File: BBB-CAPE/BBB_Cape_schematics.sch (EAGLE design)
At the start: 81 parts, among them IC1 EEPROM-I2CSMD, SW2 219-02

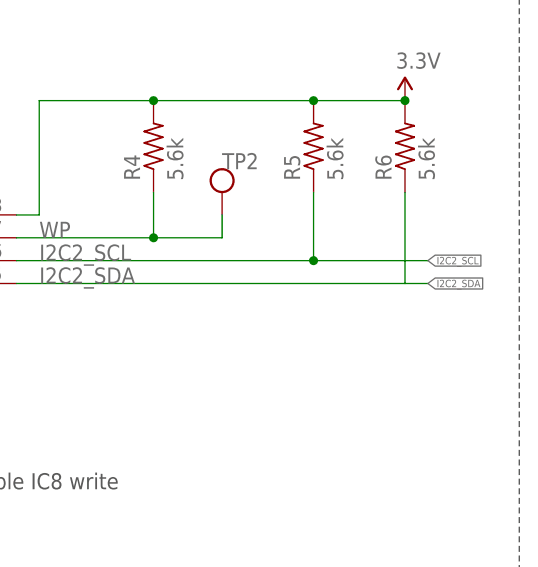
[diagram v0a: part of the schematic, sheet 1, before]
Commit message: Placement of components in BBB_Cape_schematics.brd, removed ERC erros in BBB_Cape_schematics.sch and Add sign in INA129 to identify pin no 1 in Components.lbr
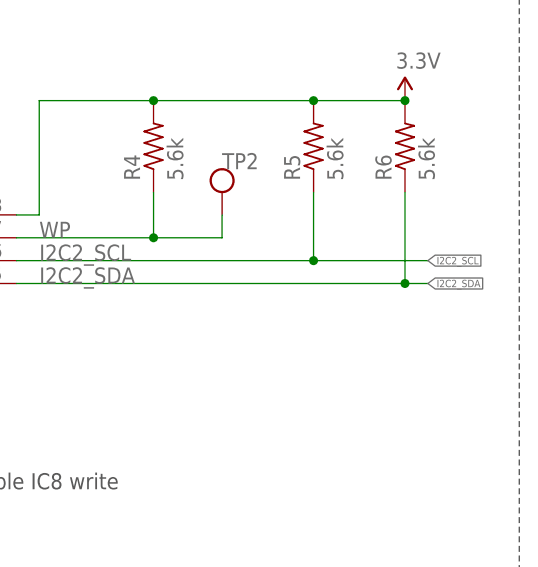
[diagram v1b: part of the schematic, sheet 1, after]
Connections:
- net N$23: now also U$17.P$1; no longer U$16.P$1
- net N$24: now also U$16.P$1; no longer U$17.P$1
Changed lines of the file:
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@@
 <setting verticaltext="up"/>
 </settings>
-<grid distance="0.1" unitdist="inch" unit="inch" style="lines" multiple="1" display="yes" altdistance="0.01" altunitdist="inch" altunit="inch"/>
+<grid distance="0.1" unitdist="inch" unit="inch" style="lines" multiple="1" display="no" altdistance="0.01" altunitdist="inch" altunit="inch"/>
 <layers>
 <layer number="1" name="Top" color="4" fill="1" visible="yes" active="no"/>
@@
 <part name="U$14" library="Components" deviceset="LMP2021" device=""/>
 <part name="U$15" library="SparkFun-Aesthetics" deviceset="5V" device=""/>
+<part name="U$17" library="Components" deviceset="PAD" device=""/>
 <part name="U$16" library="Components" deviceset="PAD" device=""/>
-<part name="U$17" library="Components" deviceset="PAD" device=""/>
 <part name="U$18" library="Components" deviceset="PAD" device=""/>
 <part name="U$19" library="Components" deviceset="ADS1252" device=""/>
@@
 <label x="99.06" y="215.9" size="1.778" layer="95"/>
 <wire x1="96.52" y1="215.9" x2="139.7" y2="215.9" width="0.1524" layer="91"/>
+<label x="142.24" y="215.9" size="0.8128" layer="95" xref="yes"/>
 <pinref part="R6" gate="G$1" pin="1"/>
+<wire x1="139.7" y1="215.9" x2="142.24" y2="215.9" width="0.1524" layer="91"/>
 <wire x1="139.7" y1="226.06" x2="139.7" y2="215.9" width="0.1524" layer="91"/>
-<label x="142.24" y="215.9" size="0.8128" layer="95" xref="yes"/>
-<wire x1="139.7" y1="215.9" x2="142.24" y2="215.9" width="0.1524" layer="91"/>
+<junction x="139.7" y="215.9"/>
 </segment>
 </net>
@@
 <instance part="P+10" gate="1" x="307.34" y="200.66"/>
 <instance part="GND19" gate="1" x="307.34" y="160.02"/>
-<instance part="U$16" gate="G$1" x="68.58" y="205.74"/>
-<instance part="U$17" gate="G$1" x="68.58" y="170.18"/>
+<instance part="U$17" gate="G$1" x="68.58" y="205.74"/>
+<instance part="U$16" gate="G$1" x="68.58" y="170.18"/>
 <instance part="U$18" gate="G$1" x="45.72" y="50.8"/>
 <instance part="TP_ECG_LPF" gate="G$1" x="330.2" y="172.72" rot="R270"/>
@@
 </segment>
 <segment>
-<pinref part="C3" gate="G$1" pin="2"/>
-<pinref part="GND8" gate="1" pin="GND"/>
-<wire x1="121.92" y1="154.94" x2="121.92" y2="149.86" width="0.1524" layer="91"/>
-</segment>
-<segment>
 <pinref part="GND15" gate="1" pin="GND"/>
 <wire x1="213.36" y1="149.86" x2="213.36" y2="152.4" width="0.1524" layer="91"/>
@@
 <pinref part="GND27" gate="1" pin="GND"/>
 <wire x1="187.96" y1="147.32" x2="187.96" y2="144.78" width="0.1524" layer="91"/>
+</segment>
+<segment>
+<pinref part="C3" gate="G$1" pin="2"/>
+<pinref part="GND8" gate="1" pin="GND"/>
+<wire x1="121.92" y1="154.94" x2="121.92" y2="149.86" width="0.1524" layer="91"/>
 </segment>
 </net>
@@
 <net name="N$23" class="0">
 <segment>
-<pinref part="U$16" gate="G$1" pin="P$1"/>
+<pinref part="U$17" gate="G$1" pin="P$1"/>
 <pinref part="R11" gate="G$1" pin="1"/>
 <wire x1="86.36" y1="205.74" x2="91.44" y2="205.74" width="0.1524" layer="91"/>
@@
 <net name="N$24" class="0">
 <segment>
-<pinref part="U$17" gate="G$1" pin="P$1"/>
+<pinref part="U$16" gate="G$1" pin="P$1"/>
 <pinref part="R12" gate="G$1" pin="1"/>
 <wire x1="86.36" y1="170.18" x2="91.44" y2="170.18" width="0.1524" layer="91"/>

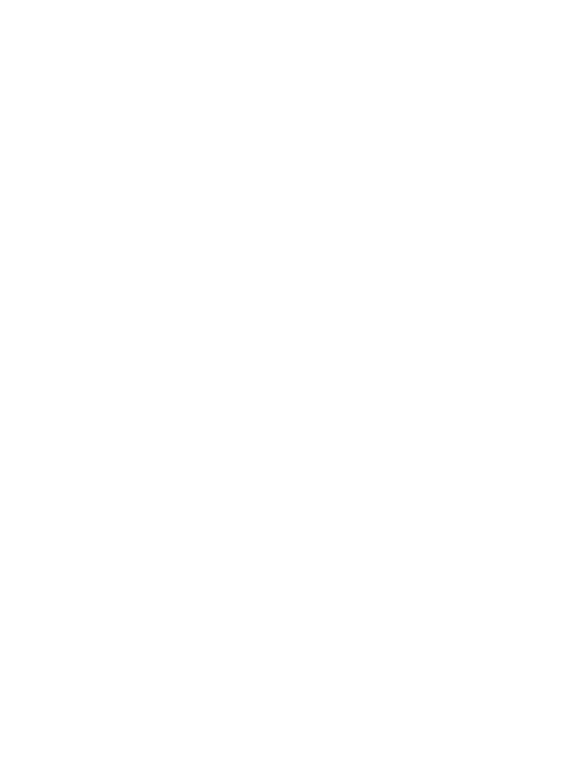
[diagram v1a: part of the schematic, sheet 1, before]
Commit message: Add 4D LCD to BBB_Cape_schematics.sch
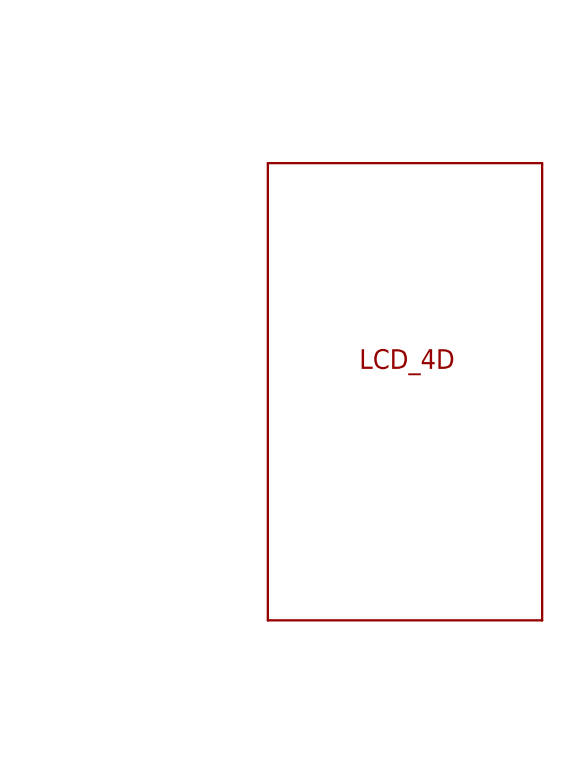
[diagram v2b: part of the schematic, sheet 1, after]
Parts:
- added U$25: LCD_4D, Components:LCD_4D
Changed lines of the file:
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@@
 <setting verticaltext="up"/>
 </settings>
-<grid distance="0.1" unitdist="inch" unit="inch" style="lines" multiple="1" display="no" altdistance="0.01" altunitdist="inch" altunit="inch"/>
+<grid distance="0.1" unitdist="inch" unit="inch" style="lines" multiple="1" display="yes" altdistance="0.01" altunitdist="inch" altunit="inch"/>
 <layers>
 <layer number="1" name="Top" color="4" fill="1" visible="yes" active="no"/>
@@
 <part name="C12" library="rcl" deviceset="C-US" device="C1206" value="0.10uF"/>
 <part name="GND30" library="supply1" deviceset="GND" device=""/>
+<part name="U$25" library="Components" deviceset="LCD_4D" device=""/>
 </parts>
 <sheets>
@@
 </instance>
 <instance part="SW2" gate="G$1" x="33.02" y="210.82" rot="R270"/>
+<instance part="U$25" gate="G$1" x="269.24" y="142.24"/>
 </instances>
 <busses>

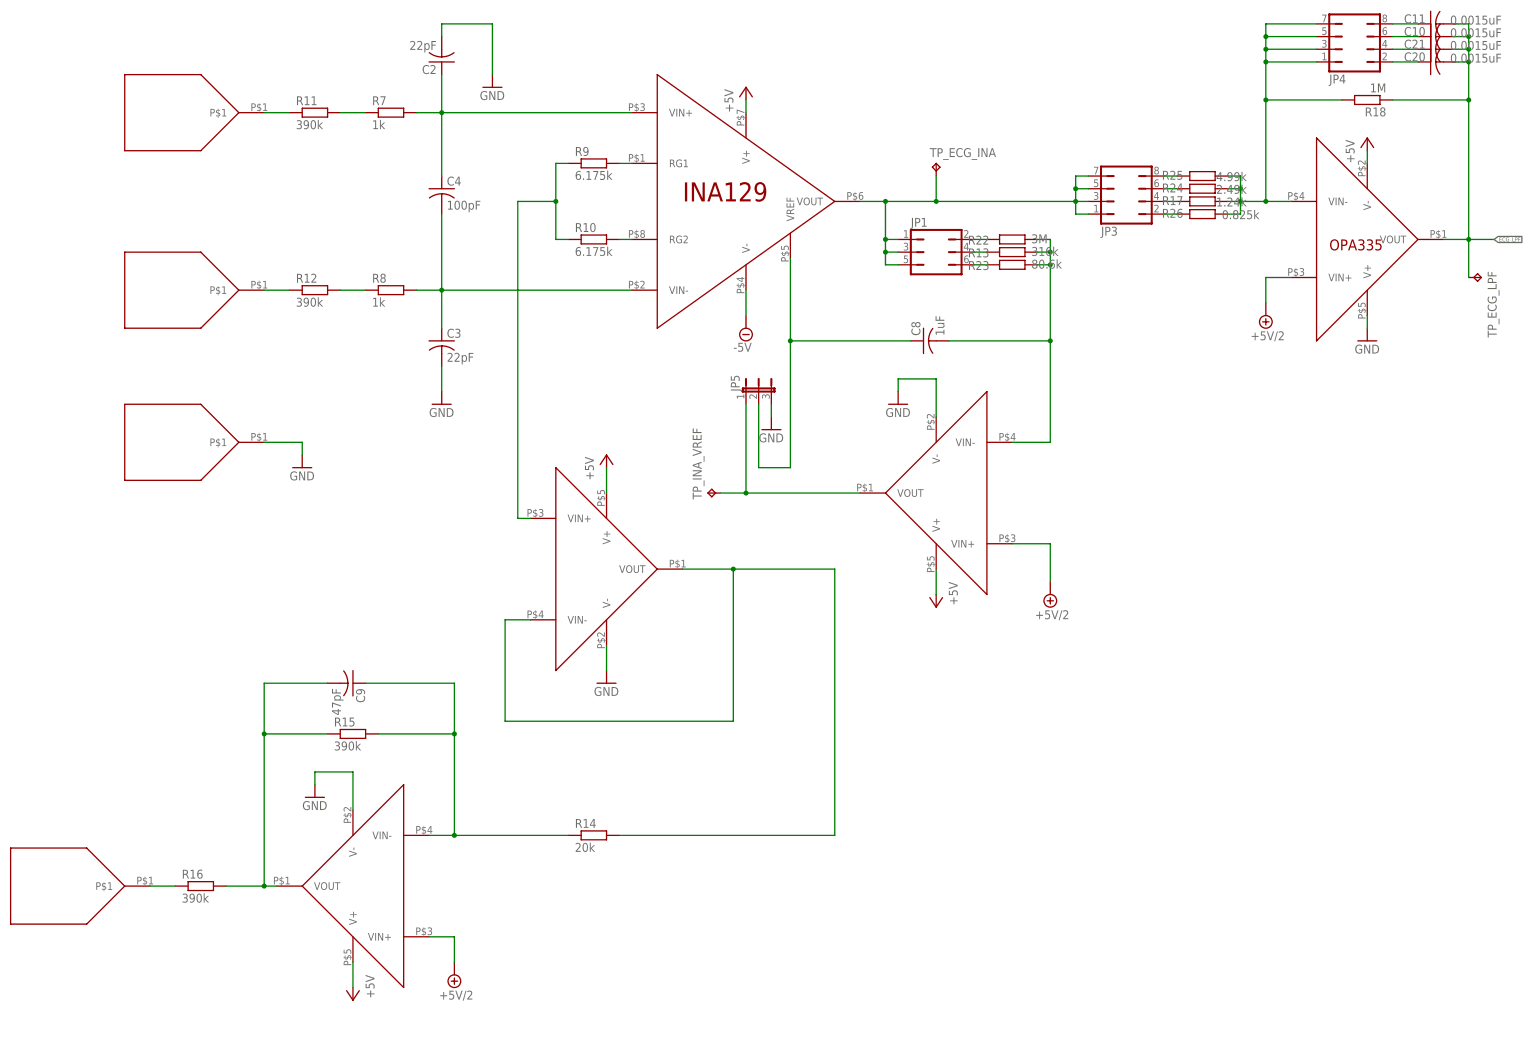
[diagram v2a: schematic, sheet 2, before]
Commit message: Replace all LMP2021 with OPA335 in BBB_Cape_schematics.sch
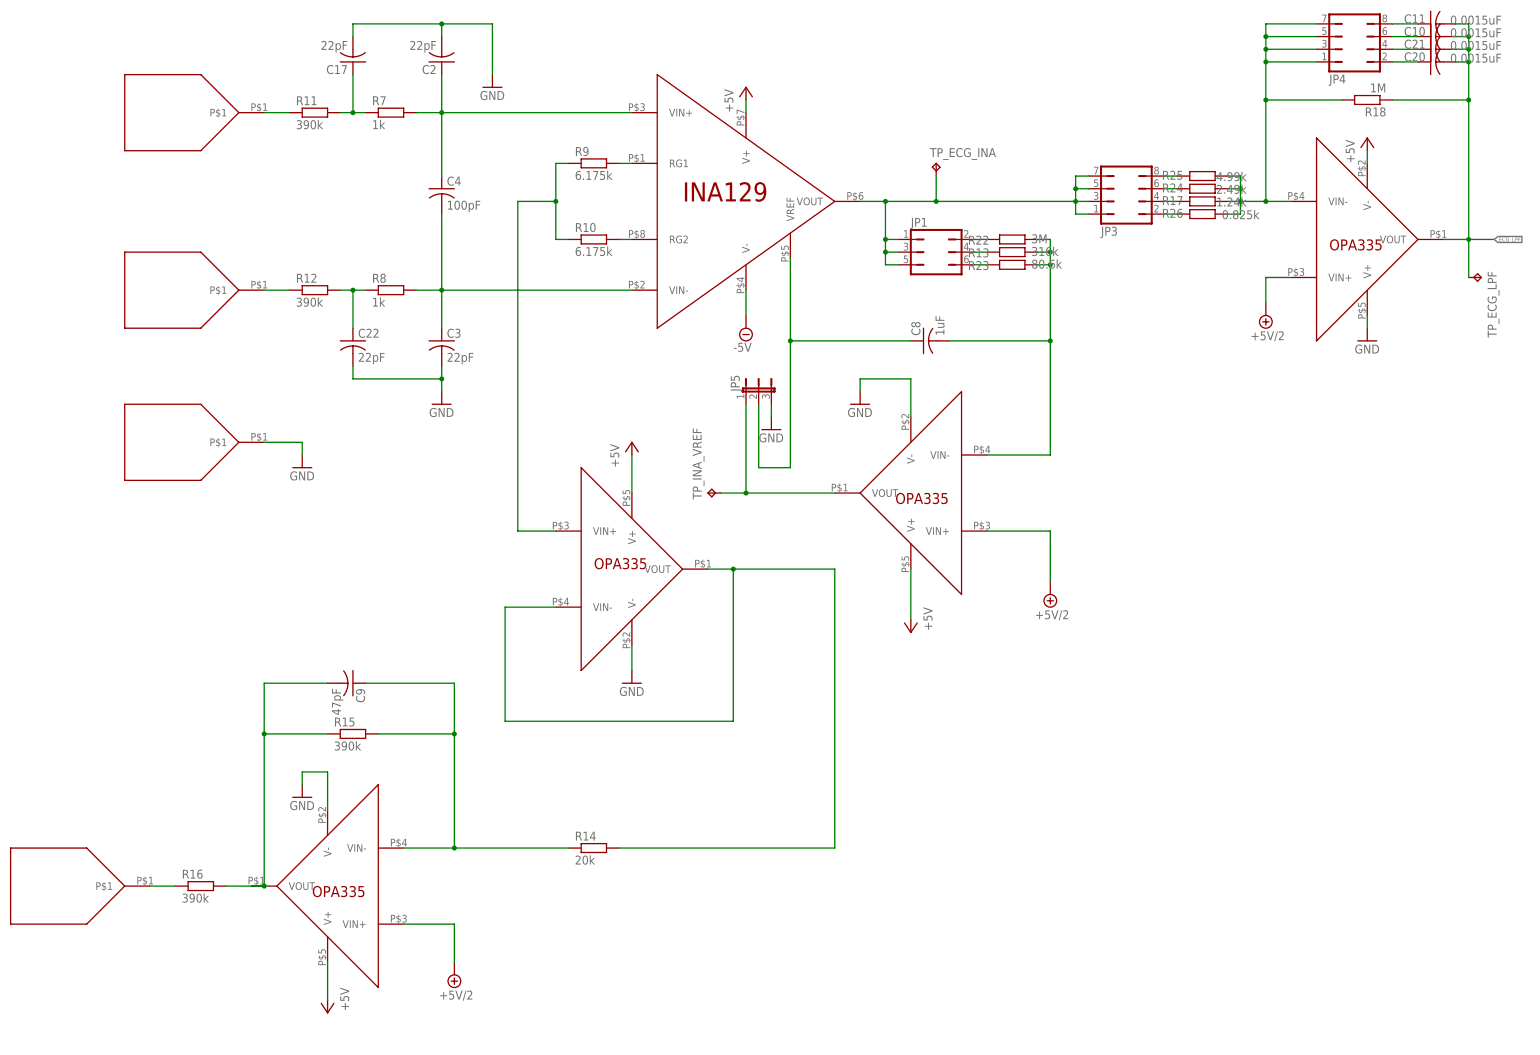
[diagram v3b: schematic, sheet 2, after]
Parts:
- added C17, C22: 22pF, rcl:C-USC1206
- U$11, U$12, U$14, U$9: value LMP2021 -> OPA335; device Components:LMP2021 -> Components:OPA335
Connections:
- net GND: now also C17.2, C22.2
- net N$7: now also C17.1
- net N$8: now also C22.1
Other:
- moved on the sheet: R14, TP2_MIN5V

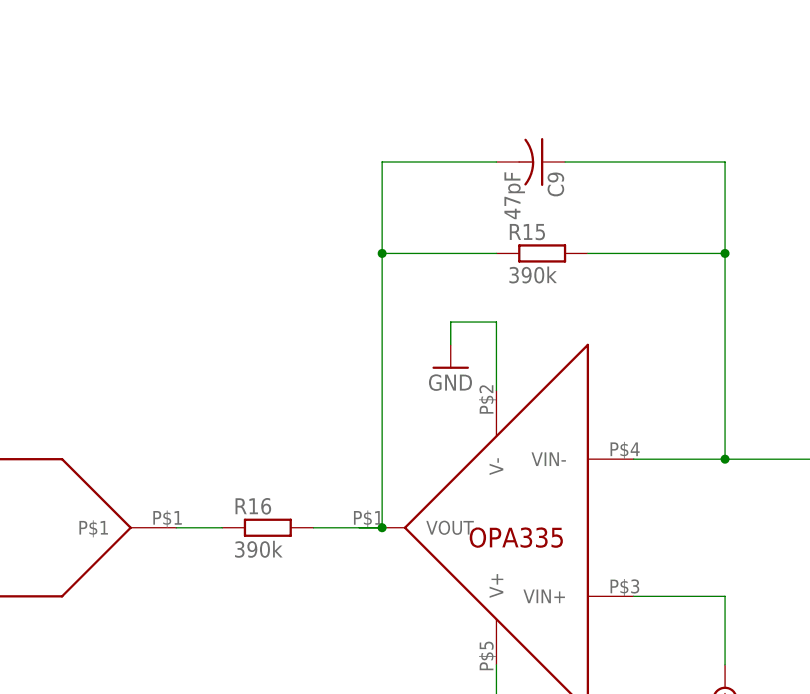
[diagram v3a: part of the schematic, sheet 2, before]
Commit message: Change +5V signal to 5V signal in BBB_Cape_schematics.sch and Update 12MHz crystal package in BBB_Cape_schematics.brd
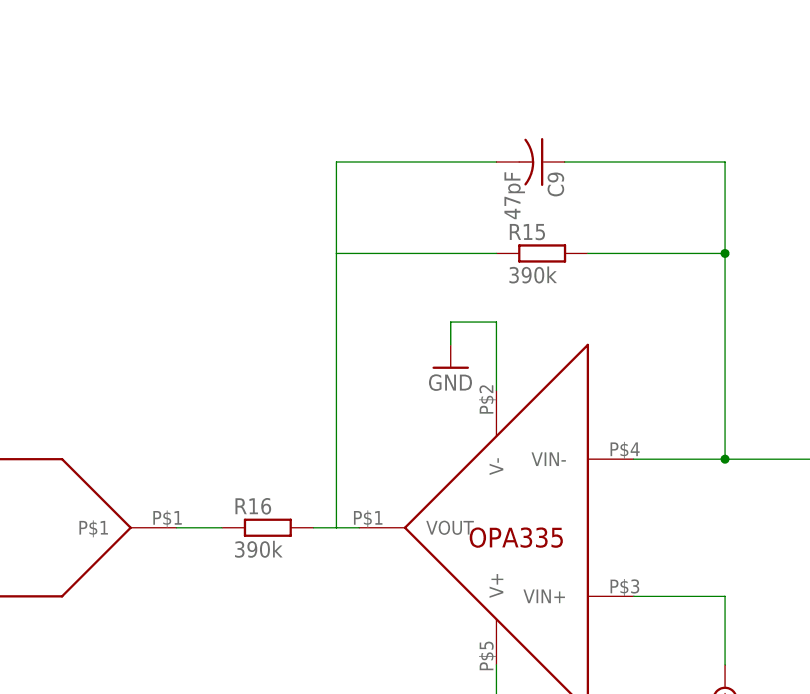
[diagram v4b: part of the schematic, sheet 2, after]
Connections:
- net +5V: no longer C13.1, U$21.VIN
- net 5V: now also C13.1, U$21.VIN
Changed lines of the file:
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@@
 <setting verticaltext="up"/>
 </settings>
-<grid distance="0.1" unitdist="inch" unit="inch" style="lines" multiple="1" display="yes" altdistance="0.01" altunitdist="inch" altunit="inch"/>
+<grid distance="0.1" unitdist="inch" unit="inch" style="lines" multiple="1" display="no" altdistance="0.01" altunitdist="inch" altunit="inch"/>
 <layers>
 <layer number="1" name="Top" color="4" fill="1" visible="no" active="no"/>
@@
 <part name="U$21" library="Components" deviceset="REF3125" device=""/>
 <part name="U$22" library="Components" deviceset="OPA335" device=""/>
-<part name="P+11" library="supply1" deviceset="+5V" device=""/>
 <part name="GND21" library="supply1" deviceset="GND" device=""/>
 <part name="C13" library="rcl" deviceset="C-US" device="C1206" value="0.1uF"/>
@@
 <part name="C17" library="rcl" deviceset="C-US" device="C1206" value="22pF"/>
 <part name="C22" library="rcl" deviceset="C-US" device="C1206" value="22pF"/>
+<part name="U$26" library="SparkFun-Aesthetics" deviceset="5V" device=""/>
 </parts>
 <sheets>
@@
 <wire x1="124.46" y1="58.42" x2="147.32" y2="58.42" width="0.1524" layer="91"/>
 <junction x="124.46" y="58.42"/>
-</segment>
-</net>
-<net name="N$19" class="0">
-<segment>
-<pinref part="U$12" gate="G$1" pin="VOUT"/>
-<pinref part="R16" gate="G$1" pin="2"/>
-<wire x1="83.82" y1="50.8" x2="86.36" y2="50.8" width="0.1524" layer="91"/>
-<pinref part="R15" gate="G$1" pin="1"/>
-<wire x1="86.36" y1="50.8" x2="78.74" y2="50.8" width="0.1524" layer="91"/>
-<wire x1="99.06" y1="81.28" x2="86.36" y2="81.28" width="0.1524" layer="91"/>
-<wire x1="86.36" y1="81.28" x2="86.36" y2="50.8" width="0.1524" layer="91"/>
-<junction x="86.36" y="50.8"/>
-<pinref part="C9" gate="G$1" pin="2"/>
-<wire x1="99.06" y1="91.44" x2="86.36" y2="91.44" width="0.1524" layer="91"/>
-<wire x1="86.36" y1="91.44" x2="86.36" y2="81.28" width="0.1524" layer="91"/>
-<junction x="86.36" y="81.28"/>
 </segment>
 </net>
@@
 </segment>
 </net>
+<net name="N$19" class="0">
+<segment>
+<pinref part="R16" gate="G$1" pin="2"/>
+<pinref part="U$12" gate="G$1" pin="VOUT"/>
+<wire x1="78.74" y1="50.8" x2="81.28" y2="50.8" width="0.1524" layer="91"/>
+<pinref part="C9" gate="G$1" pin="2"/>
+<wire x1="81.28" y1="50.8" x2="83.82" y2="50.8" width="0.1524" layer="91"/>
+<wire x1="99.06" y1="91.44" x2="81.28" y2="91.44" width="0.1524" layer="91"/>
+<wire x1="81.28" y1="91.44" x2="81.28" y2="81.28" width="0.1524" layer="91"/>
+<pinref part="R15" gate="G$1" pin="1"/>
+<wire x1="81.28" y1="81.28" x2="81.28" y2="50.8" width="0.1524" layer="91"/>
+<wire x1="99.06" y1="81.28" x2="81.28" y2="81.28" width="0.1524" layer="91"/>
+</segment>
+</net>
 </nets>
 </sheet>
@@
 <instance part="U$21" gate="G$1" x="76.2" y="76.2"/>
 <instance part="U$22" gate="G$1" x="162.56" y="83.82" rot="MR180"/>
-<instance part="P+11" gate="1" x="53.34" y="88.9"/>
 <instance part="GND21" gate="1" x="76.2" y="53.34"/>
 <instance part="C13" gate="G$1" x="53.34" y="68.58"/>
@@
 <instance part="C12" gate="G$1" x="170.18" y="63.5" rot="R90"/>
 <instance part="GND30" gate="1" x="177.8" y="55.88"/>
+<instance part="U$26" gate="G$1" x="53.34" y="86.36"/>
 </instances>
 <busses>
@@
 <wire x1="309.88" y1="160.02" x2="309.88" y2="154.94" width="0.1524" layer="91"/>
 </segment>
-</net>
-<net name="+5V" class="0">
-<segment>
-<pinref part="P+11" gate="1" pin="+5V"/>
+<segment>
 <pinref part="C13" gate="G$1" pin="1"/>
-<wire x1="53.34" y1="86.36" x2="53.34" y2="76.2" width="0.1524" layer="91"/>
 <pinref part="U$21" gate="G$1" pin="VIN"/>
 <wire x1="53.34" y1="76.2" x2="53.34" y2="71.12" width="0.1524" layer="91"/>
 <wire x1="60.96" y1="76.2" x2="53.34" y2="76.2" width="0.1524" layer="91"/>
+<pinref part="U$26" gate="G$1" pin="5V"/>
+<wire x1="53.34" y1="86.36" x2="53.34" y2="76.2" width="0.1524" layer="91"/>
 <junction x="53.34" y="76.2"/>
 </segment>
+</net>
+<net name="+5V" class="0">
 <segment>
 <pinref part="U$22" gate="G$1" pin="V+"/>
